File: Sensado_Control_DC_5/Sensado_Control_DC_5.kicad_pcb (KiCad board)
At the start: 2 copper layers, 100 x 100 mm, 91 parts, among them J1 Jumper, J2 Jumper, J3 Jumper, P1 R_FUENTE_CON, P10 GPIO, P2 I_+, P3 I_-, P4 POWER, P5 RS-232, P6 I2C, P7 SPI, P8 GND_REG, P9 RESET, Q1 NMOS, Q10 PMOS, Q11 NMOS, Q12 NMOS, Q13 NMOS, Q14 PMOS, Q15 PMOS, Q16 PMOS, Q2 NMOS, Q3 NMOS, Q4 NMOS, Q5 NMOS, Q6 PMOS, Q7 PMOS, Q8 PMOS, Q9 PMOS, U1 Atmega328PA, U2 ACS_712, U3 LD1117S50TR_FINAL

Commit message: PCB version final preliminar
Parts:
- added Y1: XRCHA_16M, Huellas:Crystal_SMD_XRCHA_Murata_Serie_W2,5mm_L2,0mm, F.Cu at (142.8, 138.6)
- C7, C8: value 18pF -> 8pF
- U1: footprint Housings_QFP:LQFP-32_7x7mm_Pitch0.8mm -> Housings_QFP:TQFP-32_7x7mm_Pitch0.8mm
- moved C7 7.97 mm to (140.1, 136.3), turned to 90 degrees
- moved C8 7.86 mm to (140.1, 140.9), turned to 270 degrees
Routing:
- net /5V: track 201.7 -> 212.5 mm, vias 7 -> 18
- net /CLK1: track 5.59 -> 13.2 mm
- net /CLK2: track 5.75 -> 13.2 mm
- net /GND: track 77.2 -> 80.4 mm, vias 21 -> 23
- added copper zone on F.Cu, net (none)
- added copper zone on F.Cu, net /5V
- added copper zone on F.Cu, net /GND
- added copper zone on F.Cu, net /V_FUENTE

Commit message: PCB mejorada
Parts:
- added R48: 10K, Resistors_SMD:R_0805_HandSoldering, F.Cu at (143.3, 58.6)
- added R49: 10K, Resistors_SMD:R_0805_HandSoldering, F.Cu at (143.2, 74.0)
- added R50: 10K, Resistors_SMD:R_0805_HandSoldering, F.Cu at (143.2, 90.1)
- added R51: 10K, Resistors_SMD:R_0805_HandSoldering, F.Cu at (143.2, 105.9)
- added R52: 10K, Resistors_SMD:R_0805_HandSoldering, F.Cu at (107.0, 58.5)
- added R53: 10K, Resistors_SMD:R_0805_HandSoldering, F.Cu at (107.1, 74.0)
- added R54: 10K, Resistors_SMD:R_0805_HandSoldering, F.Cu at (107.0, 90.1)
- added R55: 10K, Resistors_SMD:R_0805_HandSoldering, F.Cu at (107.3, 105.9)
- P10: footprint Socket_Strips:Socket_Strip_Straight_1x05_Pitch2.54mm -> Socket_Strips:Socket_Strip_Straight_1x03_Pitch2.54mm
- moved P1 0.84 mm to (138.2, 57.0)
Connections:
- U1 pad 12: /REG1_4 -> /VCONTROL_6
- U1 pad 13: /REG1_5 -> /VCONTROL_5
- U1 pad 19: /VCONTROL_6 -> Net-(U1-Pad19)
- U1 pad 22: /VCONTROL_5 -> Net-(U1-Pad22)
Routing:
- net /GND: track 80.4 -> 93.8 mm, vias 23 -> 31
- net /REG1_4: track 11.2 -> 0.00 mm
- net /VCONTROL_5: track 88.6 -> 98.9 mm
- net /REG1_5: track 9.10 -> 0.00 mm
- net /VCONTROL_6: track 34.1 -> 40.9 mm
- net /5V: track 212.5 -> 219.1 mm
- net Net-(Q12-Pad1): track 9.21 -> 12.6 mm
- net Net-(Q5-Pad1): track 9.30 -> 12.6 mm
- net Net-(Q11-Pad1): track 9.15 -> 12.4 mm
- net Net-(Q13-Pad1): track 9.46 -> 12.5 mm
- net Net-(Q3-Pad1): track 9.18 -> 12.0 mm
- net Net-(Q2-Pad1): track 9.12 -> 12.0 mm
- net Net-(Q4-Pad1): track 9.40 -> 12.1 mm
- net Net-(Q1-Pad1): track 9.21 -> 12.0 mm
- net /VOUT: track 494.1 -> 495.5 mm
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- added copper zone on F.Cu, net /I_SENS+
- added copper zone on F.Cu, net /I_SENS-

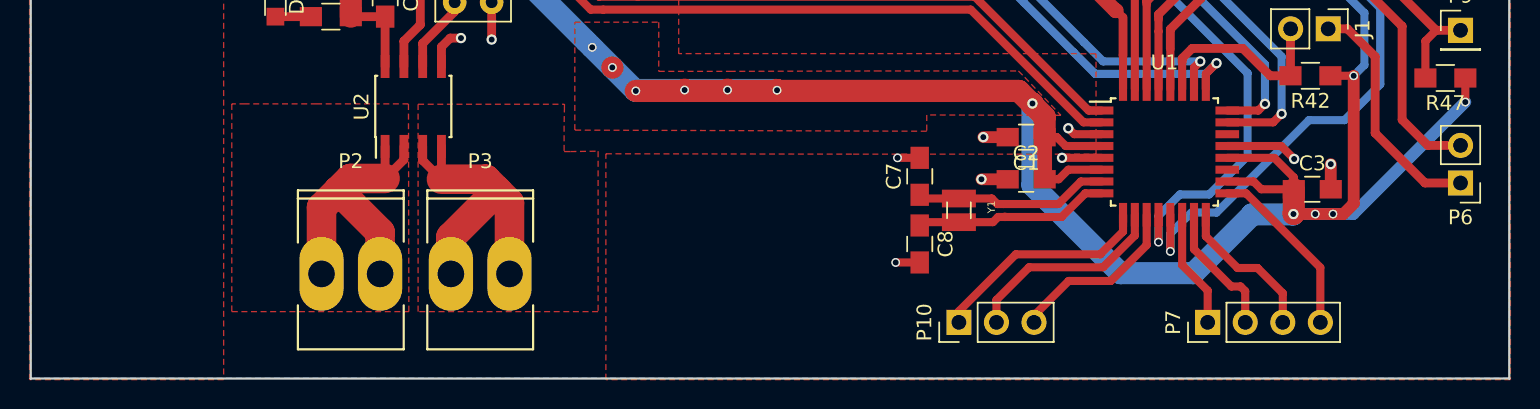
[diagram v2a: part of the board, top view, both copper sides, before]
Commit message: PCB planos del sensor de corriente actualizados
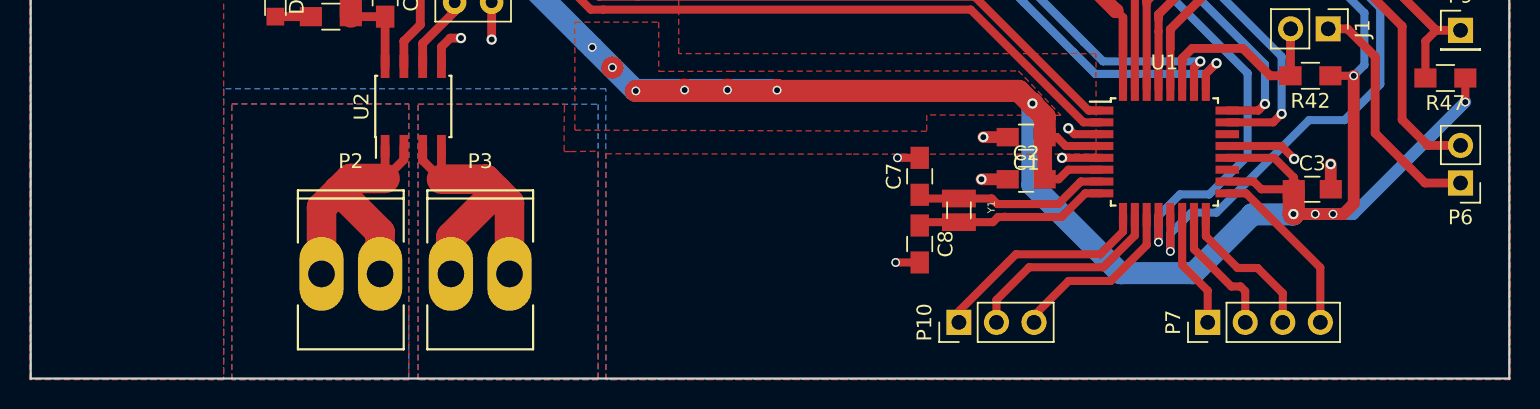
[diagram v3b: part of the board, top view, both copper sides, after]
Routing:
- added copper zone on B.Cu, net /I_SENS+
- added copper zone on B.Cu, net /I_SENS-
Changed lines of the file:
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@@
   )
   (setup
-    (last_trace_width 0.6)
+    (last_trace_width 0.25)
     (user_trace_width 0.5)
     (user_trace_width 0.55)
@@
     (polygon
       (pts
-        (xy 179.975 149.975) (xy 80.025 149.975) (xy 80.025 50.025) (xy 179.975 50.025) (xy 179.975 149.975)
+        (xy 179.975 149.975) (xy 118.9 150.075) (xy 118.9 130.4) (xy 93.05 130.4) (xy 93.05 150.075)
+        (xy 80.025 149.975) (xy 80.025 50.025) (xy 179.975 50.025) (xy 179.975 149.975)
       )
     )
@@
   )
   (zone (net 14) (net_name /I_SENS+) (layer F.Cu) (hatch edge 0.508)
-    (connect_pads (clearance 0.508))
+    (connect_pads yes (clearance 0.508))
     (min_thickness 0.254)
     (fill yes (arc_segments 16) (thermal_gap 0.508) (thermal_bridge_width 0.508))
     (polygon
       (pts
-        (xy 105.55 131.425) (xy 99.35 131.425) (xy 94.525 131.425) (xy 93.6 131.425) (xy 93.6 145.475)
-        (xy 100.7 145.475) (xy 105.575 145.475) (xy 105.55 131.425)
+        (xy 105.575 150.075) (xy 93.6 150.075) (xy 93.6 131.425) (xy 105.575 131.425) (xy 105.575 145.475)
       )
     )
   )
   (zone (net 15) (net_name /I_SENS-) (layer F.Cu) (hatch edge 0.508)
-    (connect_pads (clearance 0.508))
+    (connect_pads yes (clearance 0.508))
     (min_thickness 0.254)
     (fill yes (arc_segments 16) (thermal_gap 0.508) (thermal_bridge_width 0.508))
@@
       (pts
         (xy 116.1 131.6) (xy 116.075 132.9) (xy 116.075 134.65) (xy 116.5 134.65) (xy 118.375 134.625)
-        (xy 118.375 145.475) (xy 106.2 145.475) (xy 106.2 131.45) (xy 116.1 131.45) (xy 116.1 131.6)
+        (xy 118.375 150.075) (xy 106.2 150.075) (xy 106.2 131.45) (xy 116.1 131.45) (xy 116.1 131.6)
+      )
+    )
+  )
+  (zone (net 14) (net_name /I_SENS+) (layer B.Cu) (hatch edge 0.508)
+    (connect_pads yes (clearance 0.508))
+    (min_thickness 0.254)
+    (fill yes (arc_segments 16) (thermal_gap 0.508) (thermal_bridge_width 0.508))
+    (polygon
+      (pts
+        (xy 105.575 150.075) (xy 93.6 150.075) (xy 93.6 131.425) (xy 105.575 131.425) (xy 105.575 150.075)
+      )
+    )
+  )
+  (zone (net 15) (net_name /I_SENS-) (layer B.Cu) (hatch edge 0.508)
+    (connect_pads yes (clearance 0.508))
+    (min_thickness 0.254)
+    (fill yes (arc_segments 16) (thermal_gap 0.508) (thermal_bridge_width 0.508))
+    (polygon
+      (pts
+        (xy 118.375 150.075) (xy 106.2 150.075) (xy 106.2 131.45) (xy 118.375 131.45) (xy 118.375 150.075)
       )
     )

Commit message: Puertos I2C mejorados
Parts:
- P6: footprint Socket_Strips:Socket_Strip_Straight_1x02_Pitch2.54mm -> Socket_Strips:Socket_Strip_Straight_2x03_Pitch2.54mm
- moved P6 2.43 mm to (176.6, 134.3), turned to 0 degrees
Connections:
- P6 pad 1: /SDA -> /SCL
- P6 pad 2: /SCL -> /SDA
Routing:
- net /SCL: track 20.4 -> 25.4 mm
- net /5V: track 219.1 -> 220.9 mm

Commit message: Regletas con nobres definidos para sus respectivos pines
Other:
- board text added: "5V"
- board text added: "GND"
- board text added: "GPIO"
- board text added: "I+_SENS"
- board text added: "I-_SENS"
- board text added: "MISO"
- board text added: "MOSI"
- board text added: "RESET"
- board text added: "RX"
- board text added: "SCK"
- board text added: "SCL"
- board text added: "SDA"
- board text added: "TX"
- board text added: "V_FUENTE"
- board text added: "~SS"

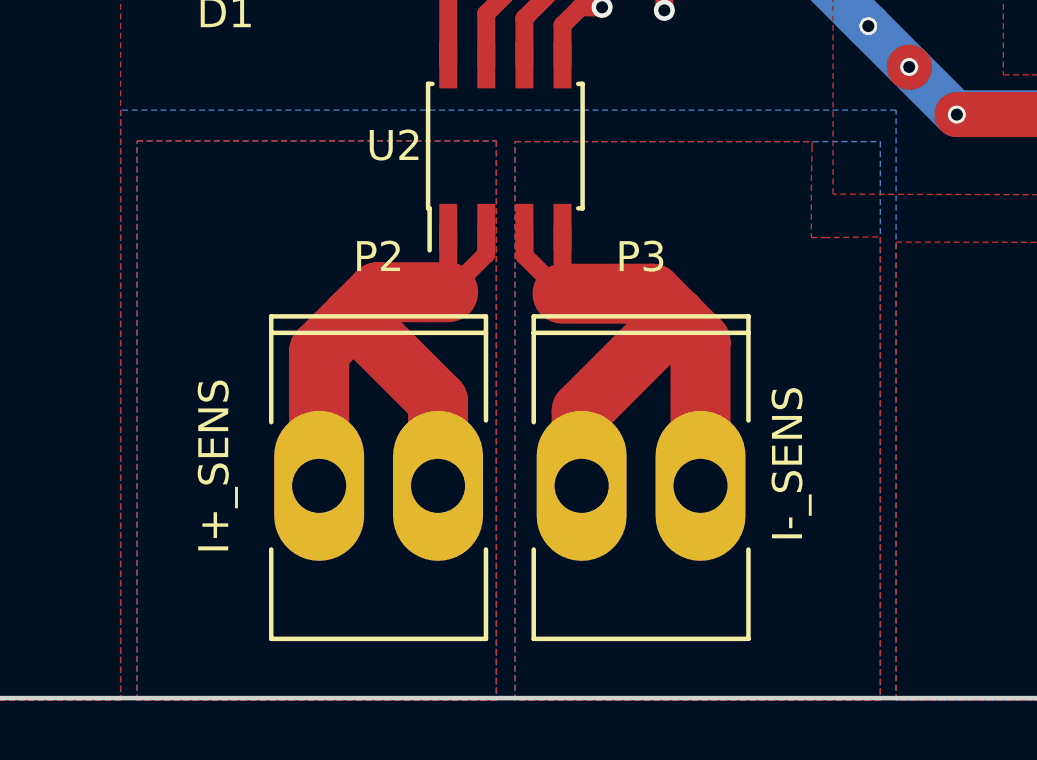
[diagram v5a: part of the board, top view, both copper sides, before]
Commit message: Vias para el sensor de corriente, PCB version final
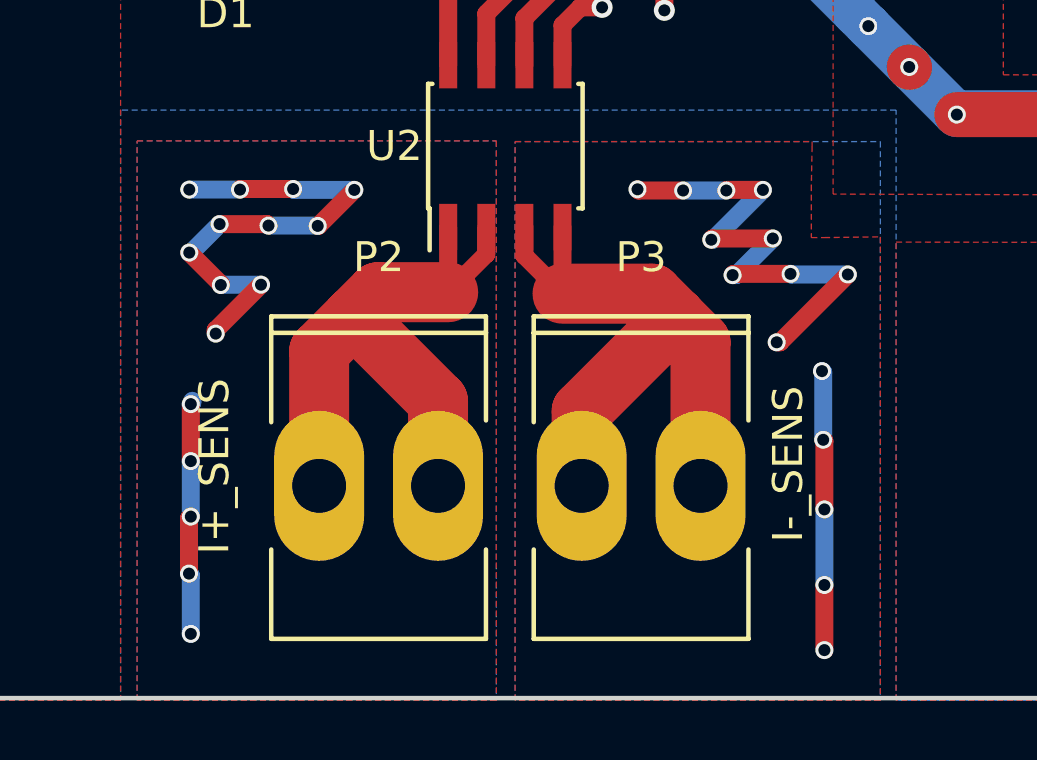
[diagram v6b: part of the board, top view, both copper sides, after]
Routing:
- net /I_SENS-: track 22.0 -> 49.0 mm, vias 0 -> 15
- net /I_SENS+: track 21.3 -> 46.2 mm, vias 0 -> 16
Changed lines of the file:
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@@
     (thickness 1.6)
     (drawings 23)
-    (tracks 831)
+    (tracks 912)
     (zones 0)
     (modules 100)
@@
   )
   (setup
-    (last_trace_width 0.25)
+    (last_trace_width 0.6)
     (user_trace_width 0.5)
     (user_trace_width 0.55)
@@
   (segment (start 135.92 83.075) (end 135.92 99.175) (width 1) (layer F.Cu) (net 13))
   (segment (start 135.92 67.6) (end 135.92 83.075) (width 1) (layer F.Cu) (net 13))
+  (segment (start 95.44 140.09) (end 95.44 140.15) (width 0.6) (layer B.Cu) (net 14))
+  (via (at 95.39 147.86) (size 0.6) (drill 0.4) (layers F.Cu B.Cu) (net 14))
+  (segment (start 95.39 145.91) (end 95.39 147.86) (width 0.6) (layer B.Cu) (net 14))
+  (segment (start 95.33 145.85) (end 95.39 145.91) (width 0.6) (layer B.Cu) (net 14))
+  (via (at 95.33 145.85) (size 0.6) (drill 0.4) (layers F.Cu B.Cu) (net 14))
+  (segment (start 95.33 144.01) (end 95.33 145.85) (width 0.6) (layer F.Cu) (net 14))
+  (segment (start 95.39 143.95) (end 95.33 144.01) (width 0.6) (layer F.Cu) (net 14))
+  (via (at 95.39 143.95) (size 0.6) (drill 0.4) (layers F.Cu B.Cu) (net 14))
+  (segment (start 95.39 142.1) (end 95.39 143.95) (width 0.6) (layer B.Cu) (net 14))
+  (via (at 95.39 142.1) (size 0.6) (drill 0.4) (layers F.Cu B.Cu) (net 14))
+  (segment (start 95.39 140.2) (end 95.39 142.1) (width 0.6) (layer F.Cu) (net 14))
+  (via (at 95.39 140.2) (size 0.6) (drill 0.4) (layers F.Cu B.Cu) (net 14))
+  (segment (start 95.44 140.15) (end 95.39 140.2) (width 0.6) (layer B.Cu) (net 14))
+  (via (at 95.34 133.05) (size 0.6) (drill 0.4) (layers F.Cu B.Cu) (net 14))
+  (via (at 96.22 137.85) (size 0.6) (drill 0.4) (layers F.Cu B.Cu) (net 14))
+  (segment (start 96.22 137.85) (end 96.22 137.73) (width 0.6) (layer F.Cu) (net 14))
+  (segment (start 97.73 136.22) (end 96.22 137.73) (width 0.6) (layer F.Cu) (net 14))
+  (via (at 97.73 136.22) (size 0.6) (drill 0.4) (layers F.Cu B.Cu) (net 14))
+  (segment (start 96.4 136.22) (end 97.73 136.22) (width 0.6) (layer B.Cu) (net 14))
+  (segment (start 96.39 136.23) (end 96.4 136.22) (width 0.6) (layer B.Cu) (net 14))
+  (via (at 96.39 136.23) (size 0.6) (drill 0.4) (layers F.Cu B.Cu) (net 14))
+  (segment (start 96.39 136.2) (end 96.39 136.23) (width 0.6) (layer F.Cu) (net 14))
+  (segment (start 95.34 135.15) (end 96.39 136.2) (width 0.6) (layer F.Cu) (net 14))
+  (via (at 95.34 135.15) (size 0.6) (drill 0.4) (layers F.Cu B.Cu) (net 14))
+  (segment (start 95.4 135.15) (end 95.34 135.15) (width 0.6) (layer B.Cu) (net 14))
+  (segment (start 96.35 134.2) (end 95.4 135.15) (width 0.6) (layer B.Cu) (net 14))
+  (via (at 96.35 134.2) (size 0.6) (drill 0.4) (layers F.Cu B.Cu) (net 14))
+  (segment (start 97.93 134.2) (end 96.35 134.2) (width 0.6) (layer F.Cu) (net 14))
+  (segment (start 97.98 134.25) (end 97.93 134.2) (width 0.6) (layer F.Cu) (net 14))
+  (via (at 97.98 134.25) (size 0.6) (drill 0.4) (layers F.Cu B.Cu) (net 14))
+  (segment (start 99.61 134.25) (end 97.98 134.25) (width 0.6) (layer B.Cu) (net 14))
+  (segment (start 99.62 134.26) (end 99.61 134.25) (width 0.6) (layer B.Cu) (net 14))
+  (via (at 99.62 134.26) (size 0.6) (drill 0.4) (layers F.Cu B.Cu) (net 14))
+  (segment (start 99.64 134.26) (end 99.62 134.26) (width 0.6) (layer F.Cu) (net 14))
+  (segment (start 100.84 133.06) (end 99.64 134.26) (width 0.6) (layer F.Cu) (net 14))
+  (via (at 100.84 133.06) (size 0.6) (drill 0.4) (layers F.Cu B.Cu) (net 14))
+  (segment (start 98.83 133.06) (end 100.84 133.06) (width 0.6) (layer B.Cu) (net 14))
+  (segment (start 98.8 133.03) (end 98.83 133.06) (width 0.6) (layer B.Cu) (net 14))
+  (via (at 98.8 133.03) (size 0.6) (drill 0.4) (layers F.Cu B.Cu) (net 14))
+  (segment (start 97.05 133.03) (end 98.8 133.03) (width 0.6) (layer F.Cu) (net 14))
+  (segment (start 97.03 133.05) (end 97.05 133.03) (width 0.6) (layer F.Cu) (net 14))
+  (via (at 97.03 133.05) (size 0.6) (drill 0.4) (layers F.Cu B.Cu) (net 14))
+  (segment (start 97.03 133.05) (end 95.34 133.05) (width 0.6) (layer B.Cu) (net 14))
   (segment (start 103.6312 142.925) (end 103.6312 140.1062) (width 2) (layer F.Cu) (net 14))
   (segment (start 103.6312 140.1062) (end 100.8125 137.2875) (width 2) (layer F.Cu) (net 14))
@@
   (segment (start 103.97 134.3) (end 103.97 136.47) (width 0.6) (layer F.Cu) (net 14))
   (segment (start 103.97 136.47) (end 103.975 136.475) (width 0.6) (layer F.Cu) (net 14))
+  (via (at 116.43 139.1) (size 0.6) (drill 0.4) (layers F.Cu B.Cu) (net 15))
+  (via (at 116.51 148.4) (size 0.6) (drill 0.4) (layers F.Cu B.Cu) (net 15))
+  (segment (start 116.51 148.4) (end 116.51 146.23) (width 0.6) (layer F.Cu) (net 15))
+  (via (at 116.51 146.23) (size 0.6) (drill 0.4) (layers F.Cu B.Cu) (net 15))
+  (segment (start 116.51 143.71) (end 116.51 146.23) (width 0.6) (layer B.Cu) (net 15))
+  (via (at 116.51 143.71) (size 0.6) (drill 0.4) (layers F.Cu B.Cu) (net 15))
+  (segment (start 116.51 141.43) (end 116.51 143.71) (width 0.6) (layer F.Cu) (net 15))
+  (segment (start 116.47 141.39) (end 116.51 141.43) (width 0.6) (layer F.Cu) (net 15))
+  (via (at 116.47 141.39) (size 0.6) (drill 0.4) (layers F.Cu B.Cu) (net 15))
+  (segment (start 116.47 139.14) (end 116.47 141.39) (width 0.6) (layer B.Cu) (net 15))
+  (segment (start 116.47 139.14) (end 116.43 139.1) (width 0.6) (layer B.Cu) (net 15))
+  (via (at 110.28 133.04) (size 0.6) (drill 0.4) (layers F.Cu B.Cu) (net 15))
+  (via (at 114.92 138.14) (size 0.6) (drill 0.4) (layers F.Cu B.Cu) (net 15))
+  (segment (start 114.92 138.14) (end 115.03 138.14) (width 0.6) (layer F.Cu) (net 15))
+  (segment (start 117.29 135.88) (end 115.03 138.14) (width 0.6) (layer F.Cu) (net 15))
+  (via (at 117.29 135.88) (size 0.6) (drill 0.4) (layers F.Cu B.Cu) (net 15))
+  (segment (start 115.4 135.88) (end 117.29 135.88) (width 0.6) (layer B.Cu) (net 15))
+  (segment (start 115.38 135.86) (end 115.4 135.88) (width 0.6) (layer B.Cu) (net 15))
+  (via (at 115.38 135.86) (size 0.6) (drill 0.4) (layers F.Cu B.Cu) (net 15))
+  (segment (start 113.49 135.86) (end 115.38 135.86) (width 0.6) (layer F.Cu) (net 15))
+  (segment (start 113.45 135.9) (end 113.49 135.86) (width 0.6) (layer F.Cu) (net 15))
+  (via (at 113.45 135.9) (size 0.6) (drill 0.4) (layers F.Cu B.Cu) (net 15))
+  (segment (start 113.57 135.9) (end 113.45 135.9) (width 0.6) (layer B.Cu) (net 15))
+  (segment (start 114.79 134.68) (end 113.57 135.9) (width 0.6) (layer B.Cu) (net 15))
+  (via (at 114.79 134.68) (size 0.6) (drill 0.4) (layers F.Cu B.Cu) (net 15))
+  (segment (start 112.78 134.68) (end 114.79 134.68) (width 0.6) (layer F.Cu) (net 15))
+  (segment (start 112.74 134.72) (end 112.78 134.68) (width 0.6) (layer F.Cu) (net 15))
+  (via (at 112.74 134.72) (size 0.6) (drill 0.4) (layers F.Cu B.Cu) (net 15))
+  (segment (start 112.8 134.72) (end 112.74 134.72) (width 0.6) (layer B.Cu) (net 15))
+  (segment (start 114.46 133.06) (end 112.8 134.72) (width 0.6) (layer B.Cu) (net 15))
+  (via (at 114.46 133.06) (size 0.6) (drill 0.4) (layers F.Cu B.Cu) (net 15))
+  (segment (start 113.26 133.06) (end 114.46 133.06) (width 0.6) (layer F.Cu) (net 15))
+  (segment (start 113.24 133.08) (end 113.26 133.06) (width 0.6) (layer F.Cu) (net 15))
+  (via (at 113.24 133.08) (size 0.6) (drill 0.4) (layers F.Cu B.Cu) (net 15))
+  (segment (start 111.8 133.08) (end 113.24 133.08) (width 0.6) (layer B.Cu) (net 15))
+  (via (at 111.8 133.08) (size 0.6) (drill 0.4) (layers F.Cu B.Cu) (net 15))
+  (segment (start 110.32 133.08) (end 111.8 133.08) (width 0.6) (layer F.Cu) (net 15))
+  (segment (start 110.32 133.08) (end 110.28 133.04) (width 0.6) (layer F.Cu) (net 15))
   (segment (start 108.4188 142.925) (end 108.4188 140.4312) (width 2) (layer F.Cu) (net 15))
   (segment (start 108.4188 140.4312) (end 111.55 137.3) (width 2) (layer F.Cu) (net 15))

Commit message: Gerber generado
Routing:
- net (no net): track 0.00 -> 51.9 mm, vias 0 -> 31
- net /I_SENS-: track 49.0 -> 22.0 mm, vias 15 -> 0
- net /I_SENS+: track 46.2 -> 21.3 mm, vias 16 -> 0
